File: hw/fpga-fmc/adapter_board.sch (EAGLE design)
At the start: 2 parts, among them J1 5569262-1, J2 ASP-134488-01

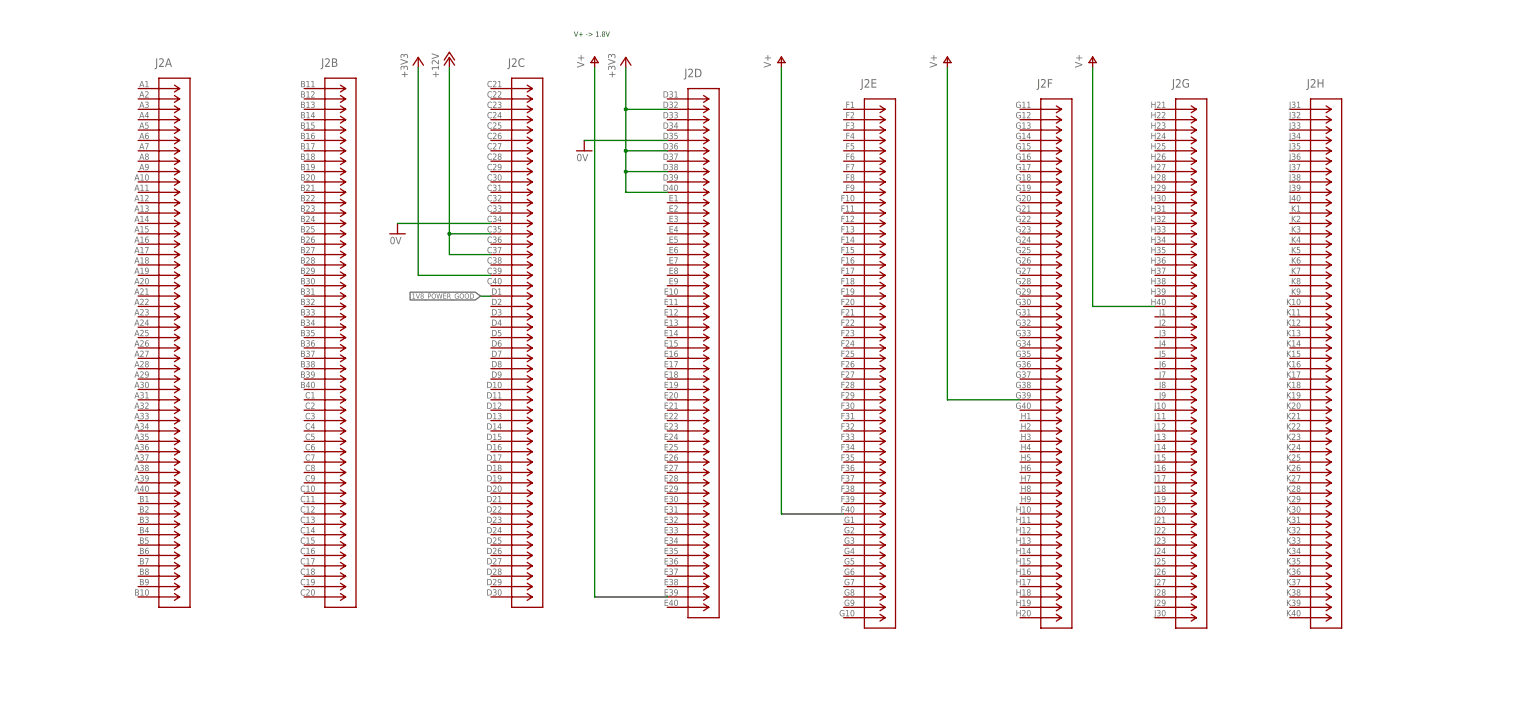
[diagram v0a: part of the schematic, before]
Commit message: fpga-fmc: add LPC pin assignment of FMC connector
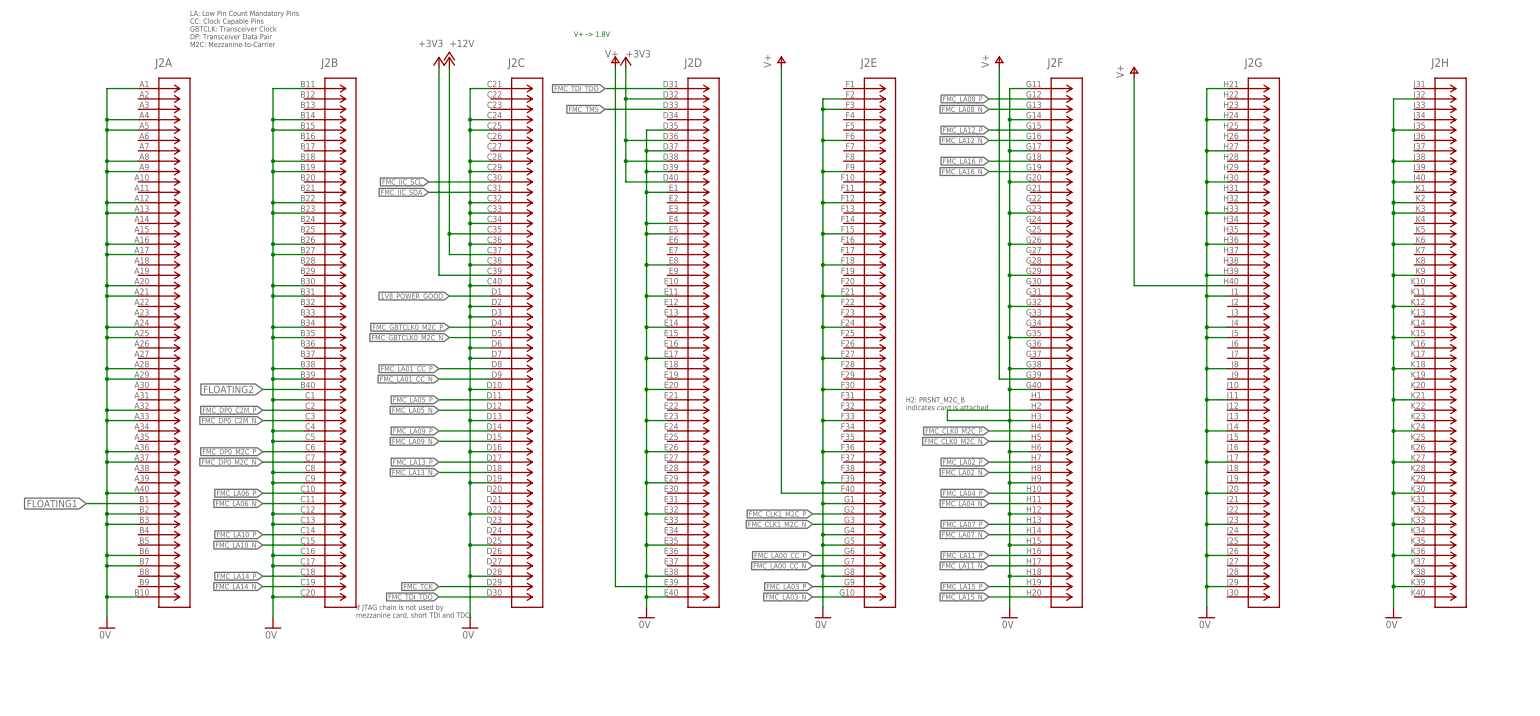
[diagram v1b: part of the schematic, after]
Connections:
- new net FLOATING1: J2A.B1
- new net FLOATING2: J2B.B40
- new net FMC_CLK0_M2C_N: J2F.H5
- new net FMC_CLK0_M2C_P: J2F.H4
- new net FMC_CLK1_M2C_N: J2E.G3
- new net FMC_CLK1_M2C_P: J2E.G2
- new net FMC_DP0_C2M_N: J2B.C3
- new net FMC_DP0_C2M_P: J2B.C2
- new net FMC_DP0_M2C_N: J2B.C7
- new net FMC_DP0_M2C_P: J2B.C6
- new net FMC_GBTCLK0_M2C_N: J2C.D5
- new net FMC_GBTCLK0_M2C_P: J2C.D4
- new net FMC_IIC_SCL: J2C.C30
- new net FMC_IIC_SDA: J2C.C31
- new net FMC_LA00_CC_N: J2E.G7
- new net FMC_LA00_CC_P: J2E.G6
- new net FMC_LA01_CC_N: J2C.D9
- new net FMC_LA01_CC_P: J2C.D8
- new net FMC_LA02_N: J2F.H8
- new net FMC_LA02_P: J2F.H7
- new net FMC_LA03_N: J2E.G10
- new net FMC_LA03_P: J2E.G9
- new net FMC_LA04_N: J2F.H11
- new net FMC_LA04_P: J2F.H10
- new net FMC_LA05_N: J2C.D12
- new net FMC_LA05_P: J2C.D11
- new net FMC_LA06_N: J2B.C11
- new net FMC_LA06_P: J2B.C10
- new net FMC_LA07_N: J2F.H14
- new net FMC_LA07_P: J2F.H13
- new net FMC_LA08_N: J2F.G13
- new net FMC_LA08_P: J2F.G12
- new net FMC_LA09_N: J2C.D15
- new net FMC_LA09_P: J2C.D14
- new net FMC_LA10_N: J2B.C15
- new net FMC_LA10_P: J2B.C14
- new net FMC_LA11_N: J2F.H17
- new net FMC_LA11_P: J2F.H16
- new net FMC_LA12_N: J2F.G16
- new net FMC_LA12_P: J2F.G15
- new net FMC_LA13_N: J2C.D18
- new net FMC_LA13_P: J2C.D17
- new net FMC_LA14_N: J2B.C19
- new net FMC_LA14_P: J2B.C18
- new net FMC_LA15_N: J2F.H20
- new net FMC_LA15_P: J2F.H19
- new net FMC_LA16_N: J2F.G19
- new net FMC_LA16_P: J2F.G18
- new net FMC_TCK: J2C.D29
- new net FMC_TDI_TDO: J2C.D30, J2D.D31
- new net FMC_TMS: J2D.D33
- net 0V: now also J2A.A1, J2A.A12, J2A.A13, J2A.A16, J2A.A17, J2A.A20, J2A.A21, J2A.A24, J2A.A25, J2A.A28, J2A.A29, J2A.A32, J2A.A33, J2A.A36, J2A.A37, J2A.A4, J2A.A40, J2A.A5, J2A.A8, J2A.A9, J2A.B10, J2A.B2, J2A.B3, J2A.B6, J2A.B7, J2B.B11, J2B.B14, J2B.B15, J2B.B18, J2B.B19, J2B.B22, J2B.B23, J2B.B26, J2B.B27, J2B.B30, J2B.B31, J2B.B34, J2B.B35, J2B.B38, J2B.B39, J2B.C1, J2B.C12, J2B.C13, J2B.C16, J2B.C17, J2B.C20, J2B.C4, J2B.C5, J2B.C8, J2B.C9, J2C.C21, J2C.C24, J2C.C25, J2C.C28, J2C.C29, J2C.C32, J2C.C33, J2C.C36, J2C.C38, J2C.C40, J2C.D10, J2C.D13, J2C.D16, J2C.D19, J2C.D2, J2C.D22, J2C.D25, J2C.D28, J2C.D3, J2C.D6, J2C.D7, J2D.D37, J2D.D39, J2D.E1, J2D.E11, J2D.E14, J2D.E17, J2D.E20, J2D.E23, J2D.E26, J2D.E29, J2D.E32, J2D.E35, J2D.E38, J2D.E4, J2D.E40, J2D.E5, J2D.E8, J2E.F12, J2E.F15, J2E.F18, J2E.F2, J2E.F21, J2E.F24, J2E.F27, J2E.F3, J2E.F30, J2E.F33, J2E.F36, J2E.F39, J2E.F6, J2E.F9, J2E.G1, J2E.G4, J2E.G5, J2E.G8, J2F.G11, J2F.G14, J2F.G17, J2F.G20, J2F.G23, J2F.G26, J2F.G29, J2F.G32, J2F.G35, J2F.G38, J2F.G40, J2F.H12, J2F.H15, J2F.H18, J2F.H2, J2F.H3, J2F.H6, J2F.H9, J2G.H21, J2G.H24, J2G.H27, J2G.H30, J2G.H33, J2G.H36, J2G.H39, J2G.J1, J2G.J11, J2G.J14, J2G.J17, J2G.J20, J2G.J23, J2G.J26, J2G.J29, J2G.J4, J2G.J5, J2G.J8, J2H.J32, J2H.J35, J2H.J38, J2H.J40, J2H.K12, J2H.K15, J2H.K18, J2H.K2, J2H.K21, J2H.K24, J2H.K27, J2H.K3, J2H.K30, J2H.K33, J2H.K36, J2H.K39, J2H.K6, J2H.K9
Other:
- note added: "H2: PRSNT_M2C_B indicates card is attached"
- note added: "LA: Low Pin Count Mandatory Pins CC: Clock Capable Pins GBTCLK: Transceiver Clock DP: Transceiver Data Pair M2C: Mezzanine-to-Carrier"
- note added: "if JTAG chain is not used by mezzanine card, short TDI and TDO."
- moved on the sheet: J2D, J2E, J2F, J2G, J2H

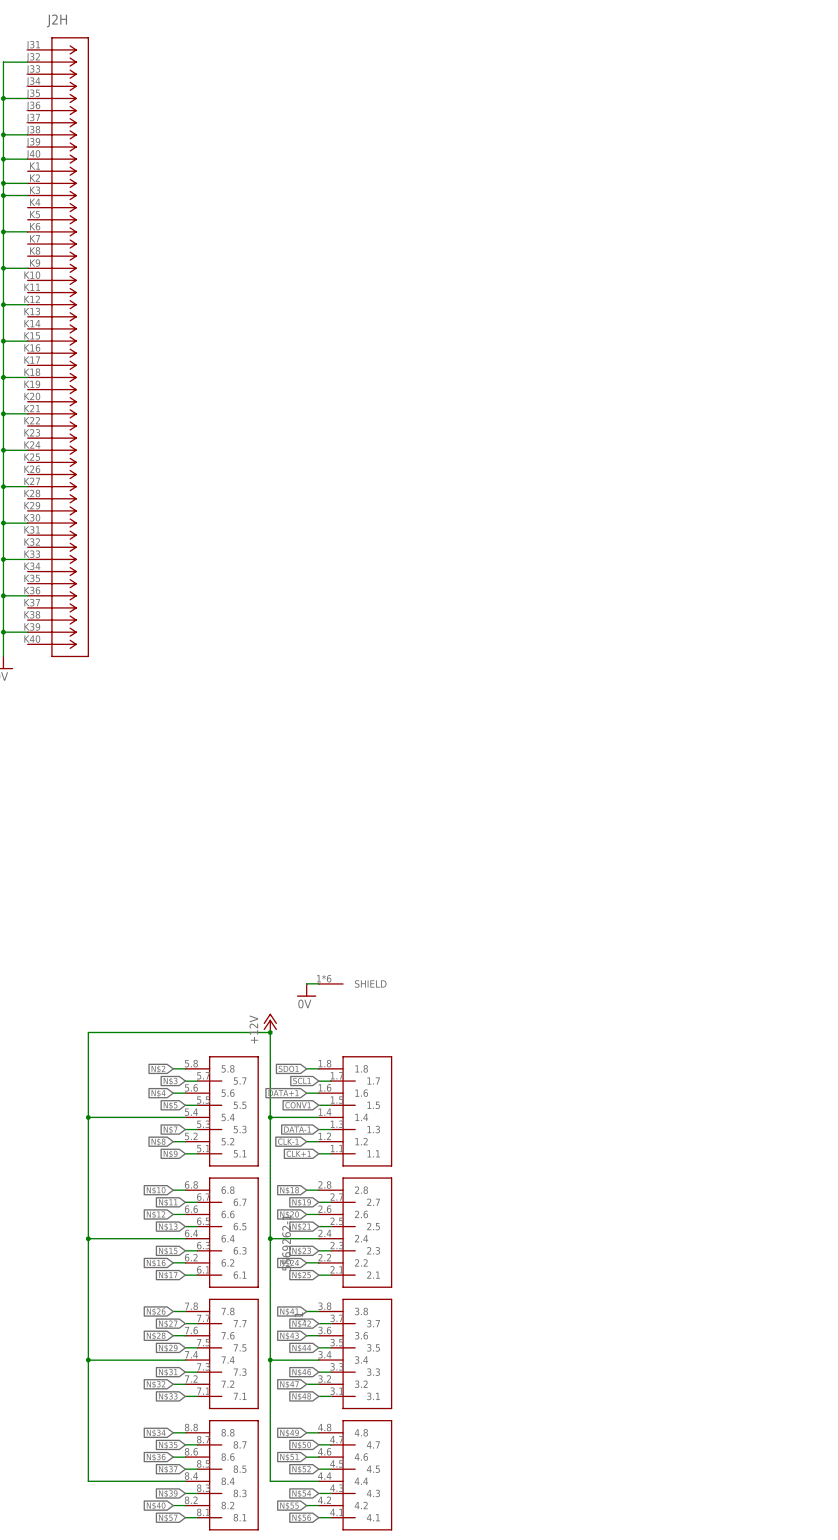
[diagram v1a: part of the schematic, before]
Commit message: fpga-fmc: fix board layout
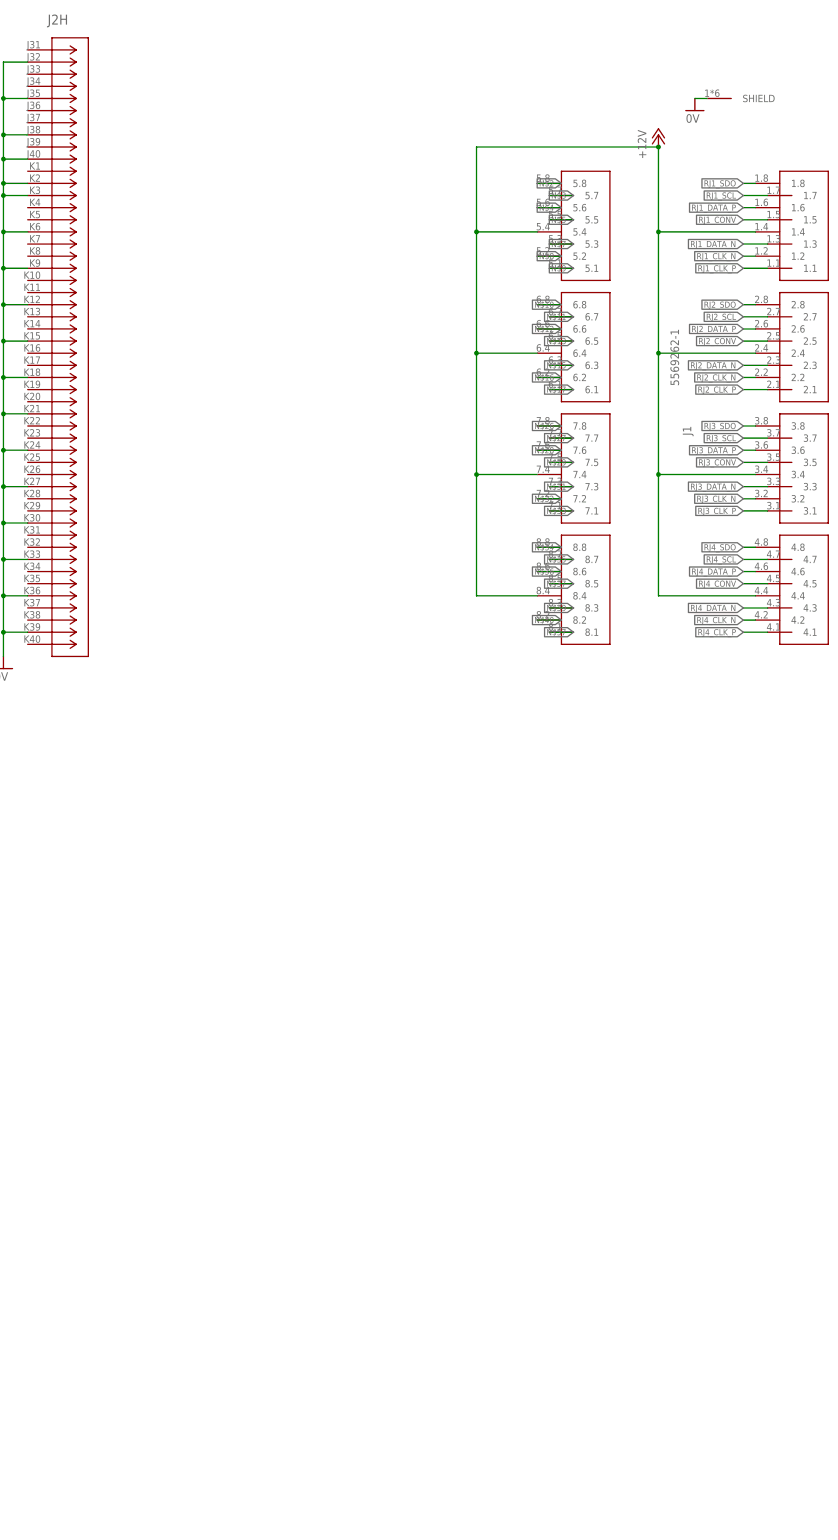
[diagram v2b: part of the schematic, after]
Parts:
- J1: device TEconnectivity_2x4_RJ45:5569262-1 -> parts:5569262-1
- J2: device myLib:ASP-134488-01 -> parts:ASP-134488-01
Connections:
- net CLK+1 renamed RJ1_CLK_P
- net CLK-1 renamed RJ1_CLK_N
- net CONV1 renamed RJ1_CONV
- net DATA+1 renamed RJ1_DATA_P
- net DATA-1 renamed RJ1_DATA_N
- net N$18 renamed RJ2_SDO
- net N$19 renamed RJ2_SCL
- net N$20 renamed RJ2_DATA_P
- net N$21 renamed RJ2_CONV
- net N$23 renamed RJ2_DATA_N
- net N$24 renamed RJ2_CLK_N
- net N$25 renamed RJ2_CLK_P
- net N$41 renamed RJ3_SDO
- net N$42 renamed RJ3_SCL
- net N$43 renamed RJ3_DATA_P
- net N$44 renamed RJ3_CONV
- net N$46 renamed RJ3_DATA_N
- net N$47 renamed RJ3_CLK_N
- net N$48 renamed RJ3_CLK_P
- net N$49 renamed RJ4_SDO
- net N$50 renamed RJ4_SCL
- net N$51 renamed RJ4_DATA_P
- net N$52 renamed RJ4_CONV
- net N$54 renamed RJ4_DATA_N
- net N$55 renamed RJ4_CLK_N
- net N$56 renamed RJ4_CLK_P
- net SCL1 renamed RJ1_SCL
- net SDO1 renamed RJ1_SDO
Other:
- moved on the sheet: J1

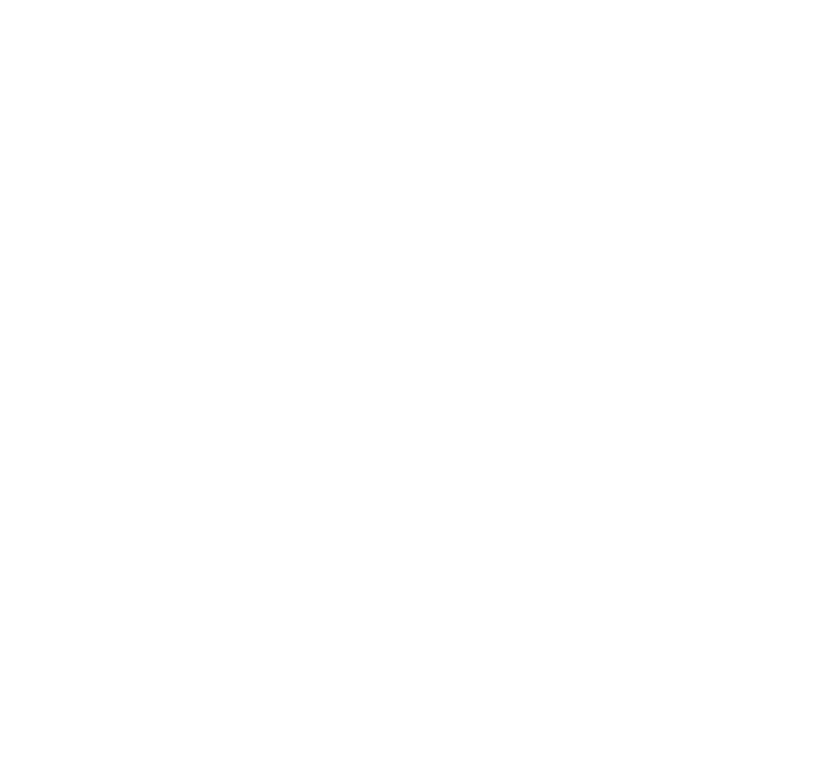
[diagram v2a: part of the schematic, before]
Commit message: fpga-fmc: add devices from analog-in pcb
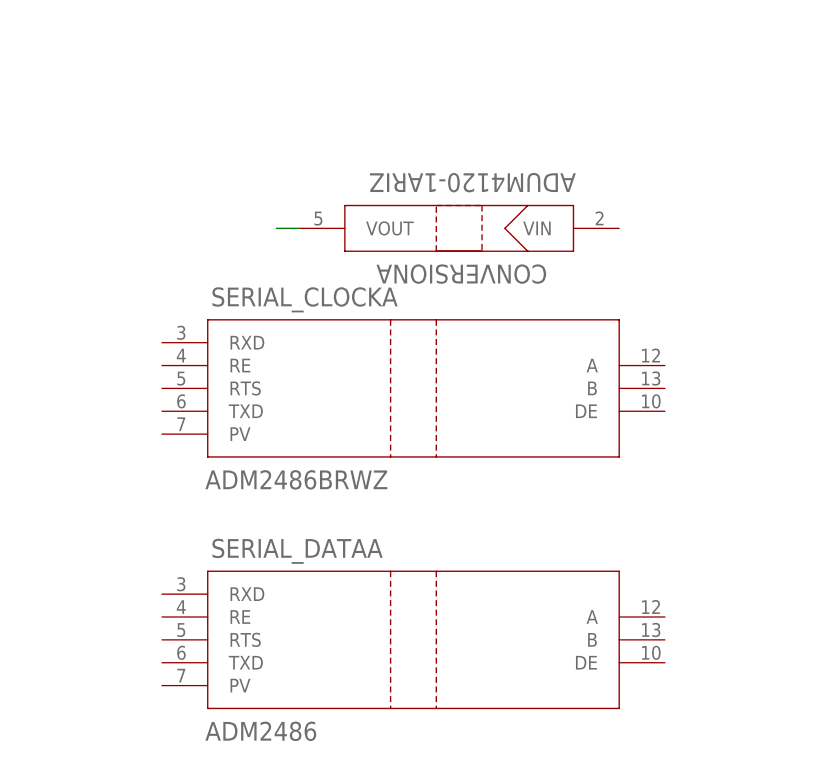
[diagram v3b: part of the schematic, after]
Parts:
- added CONVERSION: ADUM4120-1ARIZ, ADUM4120:ADUM4120-1ARIZ
- added SERIAL_CLOCK: ADM2486BRWZ, ADM2486:ADM2486BRWZ-REEL
- added SERIAL_DATA: ADM2486, ADM2486:ADM2486BRWZ-REEL
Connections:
- new net N$24: CONVERSIONA.VOUT
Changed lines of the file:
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@@
 <layer number="48" name="Document" color="7" fill="1" visible="no" active="no"/>
 <layer number="49" name="Reference" color="7" fill="1" visible="no" active="no"/>
+<layer number="50" name="dxf" color="7" fill="1" visible="no" active="no"/>
 <layer number="51" name="tDocu" color="7" fill="1" visible="no" active="no"/>
 <layer number="52" name="bDocu" color="7" fill="1" visible="no" active="no"/>
+<layer number="53" name="tGND_GNDA" color="7" fill="9" visible="no" active="no"/>
+<layer number="54" name="bGND_GNDA" color="1" fill="9" visible="no" active="no"/>
+<layer number="56" name="wert" color="7" fill="1" visible="no" active="no"/>
 <layer number="88" name="SimResults" color="9" fill="1" visible="yes" active="yes"/>
 <layer number="89" name="SimProbes" color="9" fill="1" visible="yes" active="yes"/>
@@
 <layer number="97" name="Info" color="7" fill="1" visible="yes" active="yes"/>
 <layer number="98" name="Guide" color="6" fill="1" visible="yes" active="yes"/>
+<layer number="99" name="SpiceOrder" color="5" fill="1" visible="yes" active="yes"/>
+<layer number="100" name="Muster" color="7" fill="1" visible="no" active="no"/>
+<layer number="101" name="Patch_Top" color="12" fill="4" visible="yes" active="yes"/>
+<layer number="102" name="Vscore" color="7" fill="1" visible="yes" active="yes"/>
+<layer number="103" name="tMap" color="7" fill="1" visible="yes" active="yes"/>
+<layer number="104" name="Name" color="7" fill="1" visible="yes" active="yes"/>
+<layer number="105" name="tPlate" color="7" fill="1" visible="yes" active="yes"/>
+<layer number="106" name="bPlate" color="7" fill="1" visible="yes" active="yes"/>
+<layer number="107" name="Crop" color="7" fill="1" visible="yes" active="yes"/>
+<layer number="116" name="Patch_BOT" color="9" fill="4" visible="yes" active="yes"/>
+<layer number="121" name="_tsilk" color="7" fill="1" visible="yes" active="yes"/>
+<layer number="122" name="_bsilk" color="7" fill="1" visible="yes" active="yes"/>
+<layer number="125" name="_tNames" color="7" fill="1" visible="yes" active="yes"/>
+<layer number="144" name="Drill_legend" color="7" fill="1" visible="yes" active="yes"/>
+<layer number="151" name="HeatSink" color="7" fill="1" visible="yes" active="yes"/>
+<layer number="200" name="200bmp" color="1" fill="10" visible="yes" active="yes"/>
+<layer number="201" name="201bmp" color="2" fill="1" visible="no" active="no"/>
+<layer number="202" name="202bmp" color="3" fill="1" visible="no" active="no"/>
+<layer number="203" name="203bmp" color="4" fill="10" visible="yes" active="yes"/>
+<layer number="204" name="204bmp" color="5" fill="10" visible="yes" active="yes"/>
+<layer number="205" name="205bmp" color="6" fill="10" visible="yes" active="yes"/>
+<layer number="206" name="206bmp" color="7" fill="10" visible="yes" active="yes"/>
+<layer number="207" name="207bmp" color="8" fill="10" visible="yes" active="yes"/>
+<layer number="208" name="208bmp" color="9" fill="10" visible="yes" active="yes"/>
+<layer number="209" name="209bmp" color="7" fill="1" visible="yes" active="yes"/>
+<layer number="210" name="210bmp" color="7" fill="1" visible="yes" active="yes"/>
+<layer number="211" name="211bmp" color="7" fill="1" visible="yes" active="yes"/>
+<layer number="212" name="212bmp" color="7" fill="1" visible="yes" active="yes"/>
+<layer number="213" name="213bmp" color="7" fill="1" visible="yes" active="yes"/>
+<layer number="214" name="214bmp" color="7" fill="1" visible="yes" active="yes"/>
+<layer number="215" name="215bmp" color="7" fill="1" visible="yes" active="yes"/>
+<layer number="216" name="216bmp" color="7" fill="1" visible="yes" active="yes"/>
+<layer number="250" name="Descript" color="3" fill="1" visible="no" active="no"/>
+<layer number="251" name="SMDround" color="12" fill="11" visible="no" active="no"/>
+<layer number="254" name="cooling" color="7" fill="1" visible="yes" active="yes"/>
 </layers>
 <schematic xreflabel="%F%N/%S.%C%R" xrefpart="/%S.%C%R">
@@
 <part name="GND8" library="supply1" library_urn="urn:adsk.eagle:library:371" deviceset="0V" device=""/>
 <part name="GND9" library="supply1" library_urn="urn:adsk.eagle:library:371" deviceset="0V" device=""/>
+<part name="SERIAL_CLOCK" library="ADM2486" deviceset="ADM2486BRWZ-REEL" device="" value="ADM2486BRWZ">
+<attribute name="DIGIKEY" value="ADM2486BRWZ-REELTR-ND"/>
+</part>
+<part name="SERIAL_DATA" library="ADM2486" deviceset="ADM2486BRWZ-REEL" device="" value="ADM2486">
+<attribute name="DIGIKEY" value="ADM2486BRWZ-REELTR-ND"/>
+</part>
+<part name="CONVERSION" library="ADUM4120" deviceset="ADUM4120-1ARIZ" device="">
+<attribute name="DIGIKEY" value="ADUM4120-1ARIZ-ND"/>
+</part>
 </parts>
 <sheets>
@@
 <instance part="GND9" gate="1" x="137.16" y="185.42" smashed="yes">
 <attribute name="VALUE" x="135.255" y="182.88" size="1.778" layer="96"/>
+</instance>
+<instance part="SERIAL_CLOCK" gate="A" x="83.82" y="93.98" smashed="yes">
+<attribute name="NAME" x="61.3156" y="103.0986" size="2.0828" layer="95" ratio="6" rot="SR0"/>
+<attribute name="VALUE" x="60.6806" y="82.7786" size="2.0828" layer="96" ratio="6" rot="SR0"/>
+<attribute name="DIGIKEY" x="83.82" y="93.98" size="1.778" layer="96" display="off"/>
+</instance>
+<instance part="SERIAL_DATA" gate="A" x="83.82" y="66.04" smashed="yes">
+<attribute name="NAME" x="61.3156" y="75.1586" size="2.0828" layer="95" ratio="6" rot="SR0"/>
+<attribute name="VALUE" x="60.6806" y="54.8386" size="2.0828" layer="96" ratio="6" rot="SR0"/>
+<attribute name="DIGIKEY" x="83.82" y="66.04" size="1.778" layer="96" display="off"/>
+</instance>
+<instance part="CONVERSION" gate="A" x="88.9" y="111.76" smashed="yes" rot="R180">
+<attribute name="NAME" x="98.7044" y="107.7214" size="2.0828" layer="95" ratio="6" rot="SR180"/>
+<attribute name="VALUE" x="101.8794" y="117.8814" size="2.0828" layer="96" ratio="6" rot="SR180"/>
+<attribute name="DIGIKEY" x="88.9" y="111.76" size="1.778" layer="96" rot="R180" display="off"/>
 </instance>
 </instances>
@@
 </segment>
 </net>
+<net name="N$24" class="0">
+<segment>
+<pinref part="CONVERSION" gate="A" pin="VOUT"/>
+<wire x1="71.12" y1="111.76" x2="68.58" y2="111.76" width="0.1524" layer="91"/>
+</segment>
+</net>

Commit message: fpga-fmc: add more isolator ics. add i2c switch ic
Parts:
- removed CONVERSION: ADUM4120-1ARIZ, ADUM4120:ADUM4120-1ARIZ
- removed SERIAL_CLOCK: ADM2486BRWZ, ADM2486:ADM2486BRWZ-REEL
- removed SERIAL_DATA: ADM2486, ADM2486:ADM2486BRWZ-REEL
- added U$1: PCA9548A, parts:PCA9548A
- added U1, U10, U11, U12, U13, U14, U15, U16, U2, U3, U4, U5, U6, U7, U8, U9: LTM2881, parts:LTM2881
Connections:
- removed net N$24: CONVERSIONA.VOUT
- new net 1V8: U1.VL
- new net N$18: U1.RE
- new net N$19: U1.TE
- new net N$20: U1.DE
- new net N$23: U1.DOUT
- new net N$25: U1.VCC2
- new net N$30: U1.A
- new net N$38: U1.B
- new net N$41: U1.Y
- new net N$42: U1.Z
- new net N$43: U1.SLO
- new net N$44: U1.DIN
- new net N$45: U1.GND2
- new net U1_ON: U1.ON
- net +3V3: now also U1.VCC1
- net 0V: now also U1.GND1
- net FMC_LA06_N: now also U1.DI
- net FMC_LA06_P: now also U1.RO
